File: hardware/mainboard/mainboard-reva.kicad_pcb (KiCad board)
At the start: 4 copper layers, 88 x 48 mm, 77 parts, among them J1 USB-C, J2 BATTERY, J3 SM05B-GHS-TB / ENCODER, J4 SM03B-GHS-TB / SNOOZE, J5 Molex 54550-2472 / GDEY037T03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, J6 Molex 54550-0672 / FL21 front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, J7 SPEAKER, J8 SM02B-GHS-TB / WAKE_LED, Q2 AO3400A / WAKE, U1 ESP32-S3-WROOM-1-N8, U2 BQ24074RGTR, U3 TPS62840DLCR, U4 RV-3028-C7, U5 VEML7700, U6 MAX98357AETE+T, U7 USBLC6-2SC6

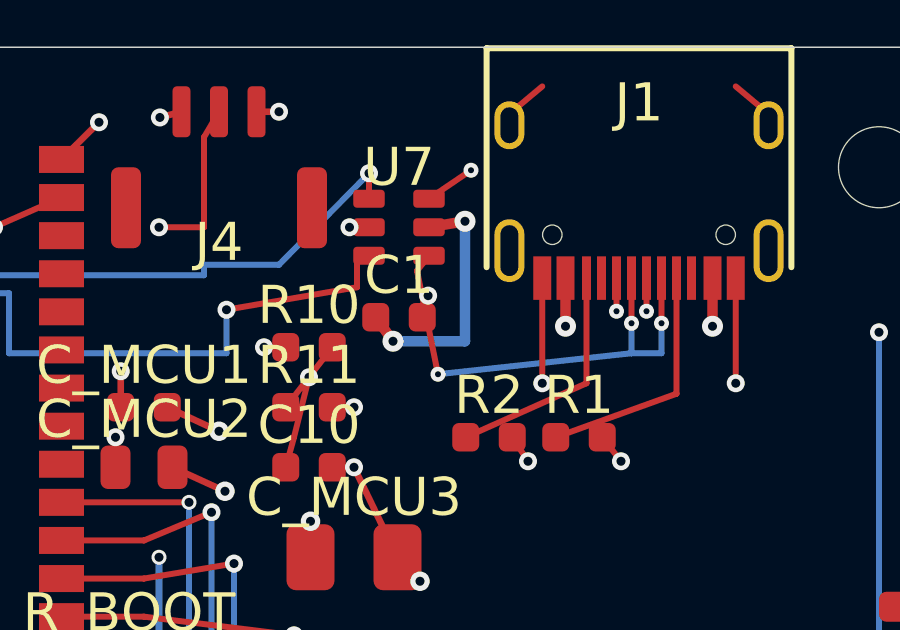
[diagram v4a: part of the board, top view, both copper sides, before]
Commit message: fix(mainboard): clear USB D- tail from local ground return
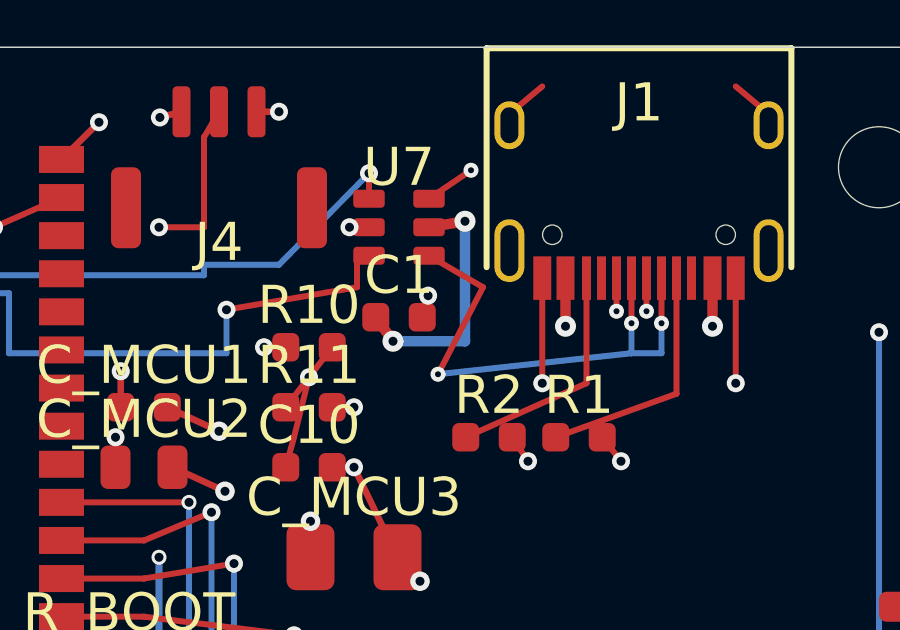
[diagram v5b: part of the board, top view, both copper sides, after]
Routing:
- net USB_D-_CONN: track 16.7 -> 17.8 mm
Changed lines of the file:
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@@
   (segment (start 75.75 10.20) (end 69.30 10.90) (width 0.20) (layer "B.Cu") (net 60))
   (via (at 69.30 10.90) (size 0.50) (drill 0.20) (layers "F.Cu" "B.Cu") (net 60))
-  (segment (start 69.30 10.90) (end 68.60 7.45) (width 0.20) (layer "F.Cu") (net 60))
-  (segment (start 68.60 7.45) (end 69.0 6.95) (width 0.20) (layer "F.Cu") (net 60))
+  (segment (start 69.30 10.90) (end 70.80 8.00) (width 0.20) (layer "F.Cu") (net 60))
+  (segment (start 70.80 8.00) (end 69.0 6.95) (width 0.20) (layer "F.Cu") (net 60))
   (segment (start 73.55 7.695) (end 73.55 9.30) (width 0.35) (layer "F.Cu") (net 2))
   (via (at 73.55 9.30) (size 0.70) (drill 0.30) (layers "F.Cu" "B.Cu") (net 2))

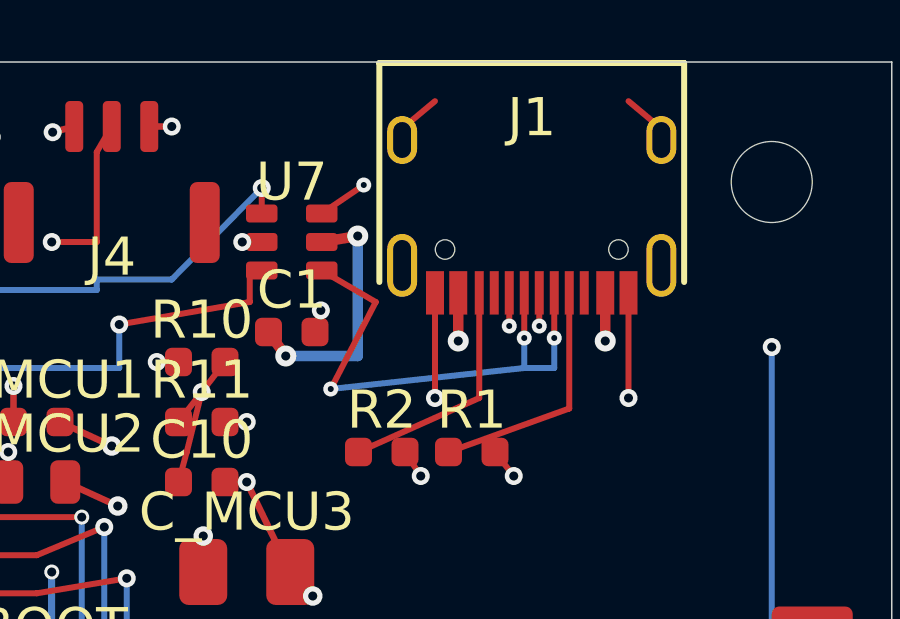
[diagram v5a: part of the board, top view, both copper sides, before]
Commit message: fix(mainboard): separate USB vias and move VBUS below breakout
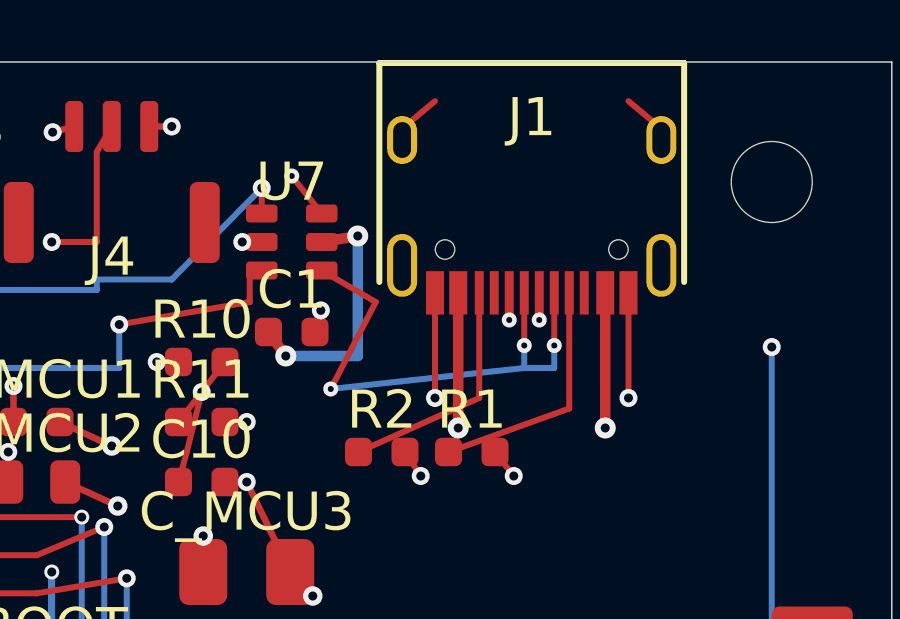
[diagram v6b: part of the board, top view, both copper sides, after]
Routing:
- net VBUS_USB: track 97.4 -> 103.4 mm
- net USB_D+_CONN: track 13.8 -> 18.1 mm
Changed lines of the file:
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@@
   (segment (start 74.775 13.00) (end 75.40 13.80) (width 0.20) (layer "F.Cu") (net 1))
   (via (at 75.40 13.80) (size 0.60) (drill 0.30) (layers "F.Cu" "B.Cu") (net 1))
-  (segment (start 75.25 7.695) (end 75.25 8.80) (width 0.20) (layer "F.Cu") (net 59))
-  (via (at 75.25 8.80) (size 0.50) (drill 0.20) (layers "F.Cu" "B.Cu") (net 59))
-  (segment (start 76.25 7.695) (end 76.25 8.80) (width 0.20) (layer "F.Cu") (net 59))
-  (via (at 76.25 8.80) (size 0.50) (drill 0.20) (layers "F.Cu" "B.Cu") (net 59))
-  (segment (start 75.25 8.80) (end 75.25 9.60) (width 0.20) (layer "In1.Cu") (net 59))
-  (segment (start 76.25 8.80) (end 76.25 9.60) (width 0.20) (layer "In1.Cu") (net 59))
-  (segment (start 76.25 9.60) (end 75.25 9.60) (width 0.20) (layer "In1.Cu") (net 59))
-  (segment (start 75.25 9.60) (end 70.40 4.10) (width 0.20) (layer "In1.Cu") (net 59))
-  (via (at 70.40 4.10) (size 0.50) (drill 0.20) (layers "F.Cu" "B.Cu") (net 59))
-  (segment (start 70.40 4.10) (end 69.0 5.05) (width 0.20) (layer "F.Cu") (net 59))
-  (segment (start 75.75 7.695) (end 75.75 9.20) (width 0.20) (layer "F.Cu") (net 60))
-  (via (at 75.75 9.20) (size 0.50) (drill 0.20) (layers "F.Cu" "B.Cu") (net 60))
-  (segment (start 76.75 7.695) (end 76.75 9.20) (width 0.20) (layer "F.Cu") (net 60))
-  (via (at 76.75 9.20) (size 0.50) (drill 0.20) (layers "F.Cu" "B.Cu") (net 60))
-  (segment (start 75.75 9.20) (end 75.75 10.20) (width 0.20) (layer "B.Cu") (net 60))
-  (segment (start 76.75 9.20) (end 76.75 10.20) (width 0.20) (layer "B.Cu") (net 60))
+  (segment (start 75.25 7.695) (end 75.25 8.60) (width 0.20) (layer "F.Cu") (net 59))
+  (via (at 75.25 8.60) (size 0.50) (drill 0.20) (layers "F.Cu" "B.Cu") (net 59))
+  (segment (start 76.25 7.695) (end 76.25 8.60) (width 0.20) (layer "F.Cu") (net 59))
+  (via (at 76.25 8.60) (size 0.50) (drill 0.20) (layers "F.Cu" "B.Cu") (net 59))
+  (segment (start 75.25 8.60) (end 75.25 9.80) (width 0.20) (layer "In1.Cu") (net 59))
+  (segment (start 76.25 8.60) (end 76.25 9.80) (width 0.20) (layer "In1.Cu") (net 59))
+  (segment (start 76.25 9.80) (end 75.25 9.80) (width 0.20) (layer "In1.Cu") (net 59))
+  (segment (start 75.25 9.80) (end 72.00 10.20) (width 0.20) (layer "In1.Cu") (net 59))
+  (segment (start 72.00 10.20) (end 68.00 6.20) (width 0.20) (layer "In1.Cu") (net 59))
+  (segment (start 68.00 6.20) (end 68.00 3.80) (width 0.20) (layer "In1.Cu") (net 59))
+  (via (at 68.00 3.80) (size 0.50) (drill 0.20) (layers "F.Cu" "B.Cu") (net 59))
+  (segment (start 68.00 3.80) (end 69.0 5.05) (width 0.20) (layer "F.Cu") (net 59))
+  (segment (start 75.75 7.695) (end 75.75 9.45) (width 0.20) (layer "F.Cu") (net 60))
+  (via (at 75.75 9.45) (size 0.50) (drill 0.20) (layers "F.Cu" "B.Cu") (net 60))
+  (segment (start 76.75 7.695) (end 76.75 9.45) (width 0.20) (layer "F.Cu") (net 60))
+  (via (at 76.75 9.45) (size 0.50) (drill 0.20) (layers "F.Cu" "B.Cu") (net 60))
+  (segment (start 75.75 9.45) (end 75.75 10.20) (width 0.20) (layer "B.Cu") (net 60))
+  (segment (start 76.75 9.45) (end 76.75 10.20) (width 0.20) (layer "B.Cu") (net 60))
   (segment (start 76.75 10.20) (end 75.75 10.20) (width 0.20) (layer "B.Cu") (net 60))
   (segment (start 75.75 10.20) (end 69.30 10.90) (width 0.20) (layer "B.Cu") (net 60))
@@
   (segment (start 69.30 10.90) (end 70.80 8.00) (width 0.20) (layer "F.Cu") (net 60))
   (segment (start 70.80 8.00) (end 69.0 6.95) (width 0.20) (layer "F.Cu") (net 60))
-  (segment (start 73.55 7.695) (end 73.55 9.30) (width 0.35) (layer "F.Cu") (net 2))
-  (via (at 73.55 9.30) (size 0.70) (drill 0.30) (layers "F.Cu" "B.Cu") (net 2))
-  (segment (start 78.45 7.695) (end 78.45 9.30) (width 0.35) (layer "F.Cu") (net 2))
-  (via (at 78.45 9.30) (size 0.70) (drill 0.30) (layers "F.Cu" "B.Cu") (net 2))
-  (segment (start 78.45 9.30) (end 73.55 9.30) (width 0.50) (layer "In2.Cu") (net 2))
-  (segment (start 73.55 9.30) (end 73.55 11.20) (width 0.50) (layer "In2.Cu") (net 2))
-  (segment (start 73.55 11.20) (end 69.80 11.20) (width 0.50) (layer "In2.Cu") (net 2))
-  (segment (start 69.80 11.20) (end 69.80 4.60) (width 0.50) (layer "In2.Cu") (net 2))
+  (segment (start 73.55 7.695) (end 73.55 12.20) (width 0.35) (layer "F.Cu") (net 2))
+  (via (at 73.55 12.20) (size 0.70) (drill 0.30) (layers "F.Cu" "B.Cu") (net 2))
+  (segment (start 78.45 7.695) (end 78.45 12.20) (width 0.35) (layer "F.Cu") (net 2))
+  (via (at 78.45 12.20) (size 0.70) (drill 0.30) (layers "F.Cu" "B.Cu") (net 2))
+  (segment (start 78.45 12.20) (end 73.55 12.20) (width 0.50) (layer "In2.Cu") (net 2))
+  (segment (start 73.55 12.20) (end 70.50 12.20) (width 0.50) (layer "In2.Cu") (net 2))
+  (segment (start 70.50 12.20) (end 70.50 3.50) (width 0.50) (layer "In2.Cu") (net 2))
+  (segment (start 70.50 3.50) (end 69.80 3.50) (width 0.50) (layer "In2.Cu") (net 2))
   (segment (start 69.0 6.0) (end 70.20 5.80) (width 0.35) (layer "F.Cu") (net 2))
   (via (at 70.20 5.80) (size 0.70) (drill 0.30) (layers "F.Cu" "B.Cu") (net 2))

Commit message: cleanup(mainboard): remove obsolete USB VBUS stub
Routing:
- net VBUS_USB: track 103.4 -> 95.4 mm
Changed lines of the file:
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@@
   (segment (start 27.95 33.0) (end 26.8 32.2) (width 0.22) (layer "F.Cu") (net 1))
   (segment (start 68.725 34.5) (end 67.9 36.7) (width 0.22) (layer "F.Cu") (net 1))
-  (segment (start 69.8 4.6) (end 77.8 4.6) (width 0.5) (layer "In2.Cu") (net 2))
   (segment (start 83.8 20.0) (end 83.0 21.75) (width 0.20) (layer "In2.Cu") (net 46))
   (segment (start 65.775 37.0) (end 65.775 40.8) (width 0.30) (layer "F.Cu") (net 41))
